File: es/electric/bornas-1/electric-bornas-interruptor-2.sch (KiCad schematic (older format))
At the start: 15 parts, among them X1 borna_12x2

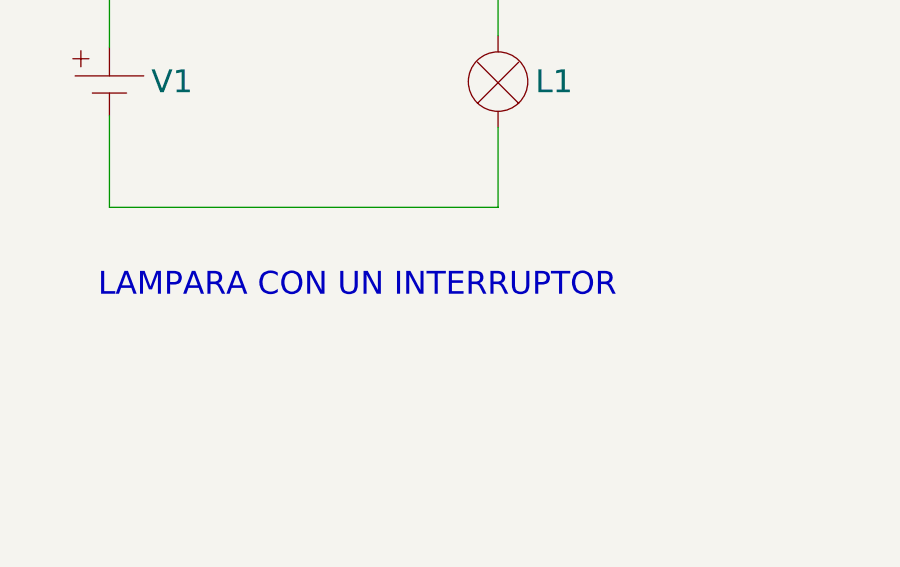
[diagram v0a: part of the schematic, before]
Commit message: Recompresión de imágenes y corrección ortográfica
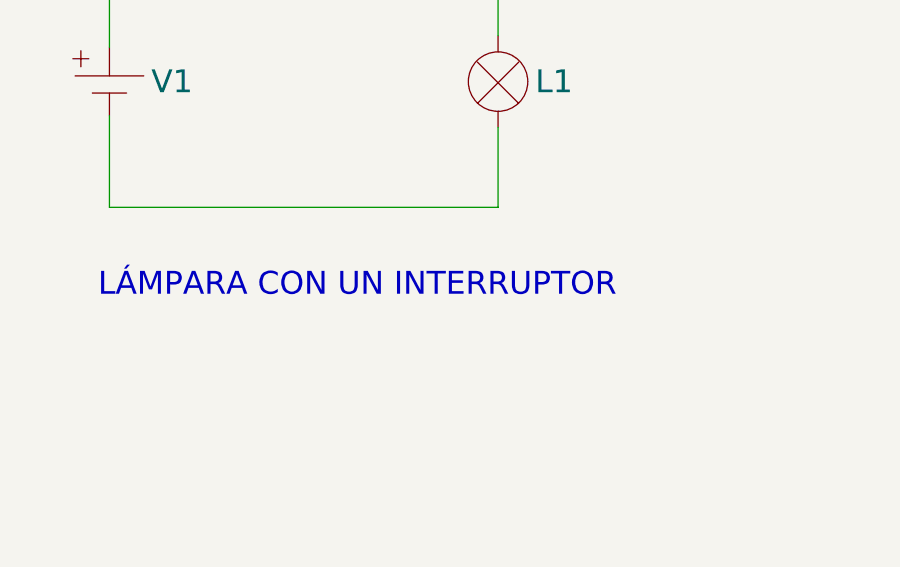
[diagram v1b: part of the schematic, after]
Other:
- note added: "LÁMPARA CON UN INTERRUPTOR"
- note removed: "LAMPARA CON UN INTERRUPTOR"
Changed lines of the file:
@@
 EESchema Schematic File Version 4
-LIBS:electric-bornas-interruptor-cache
-EELAYER 26 0
+EELAYER 30 0
 EELAYER END
 $Descr A4 8268 11693 portrait
@@
 	600  1500 1200 1500
 Text Notes 550  3000 0    100  ~ 0
-LAMPARA CON UN INTERRUPTOR
+LÁMPARA CON UN INTERRUPTOR
 $Comp
 L simbolos:borna_6x2 X?
